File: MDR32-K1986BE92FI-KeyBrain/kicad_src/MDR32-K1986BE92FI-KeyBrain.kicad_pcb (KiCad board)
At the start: 2 copper layers, 18.1 x 33.3 mm, 34 parts, among them J1 USB-C USB 2.0 MC-372, J2 SWD, U1 AP2112K-3.3, U2 USBLC6-2SC6, U3 K1986BE92FI, U4 ProMicro, Y1 8MHz

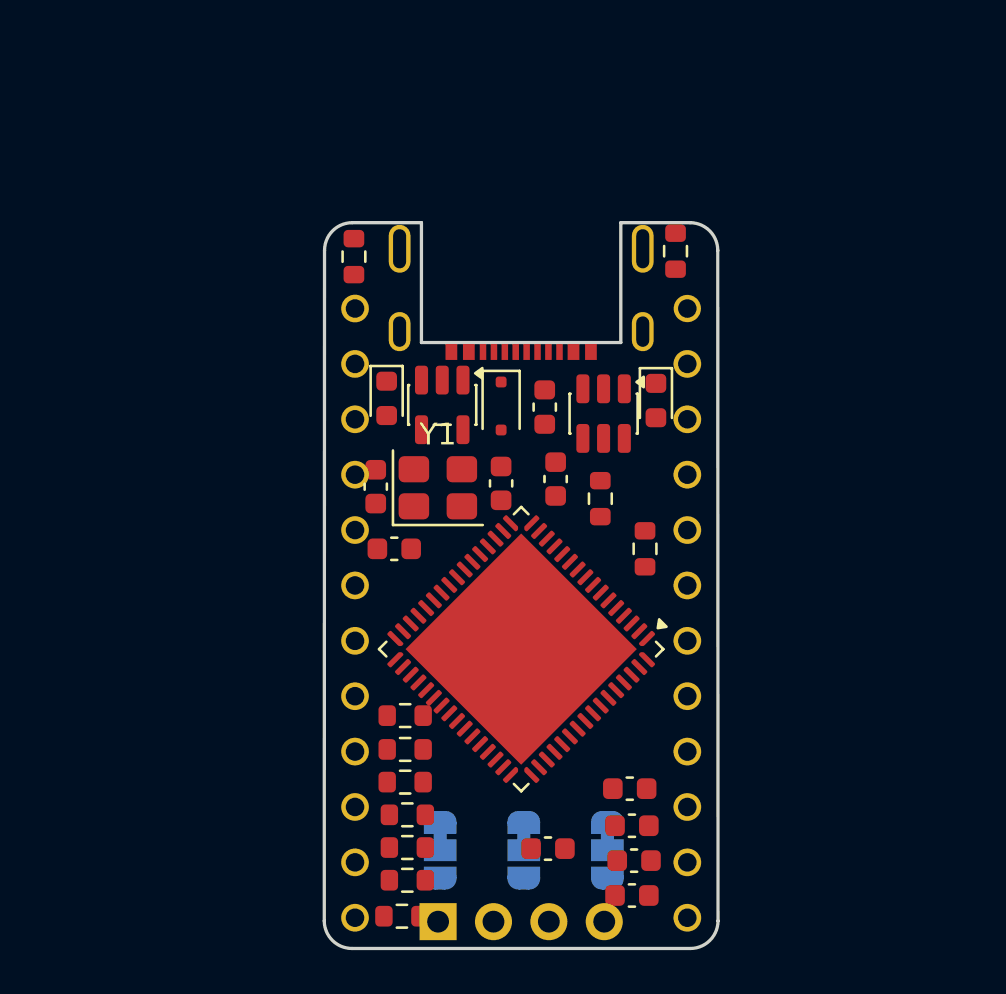
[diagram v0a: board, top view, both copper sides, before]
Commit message: MDR32-K1986BE92FI-KeyBrain: группируем и перепозиционируем
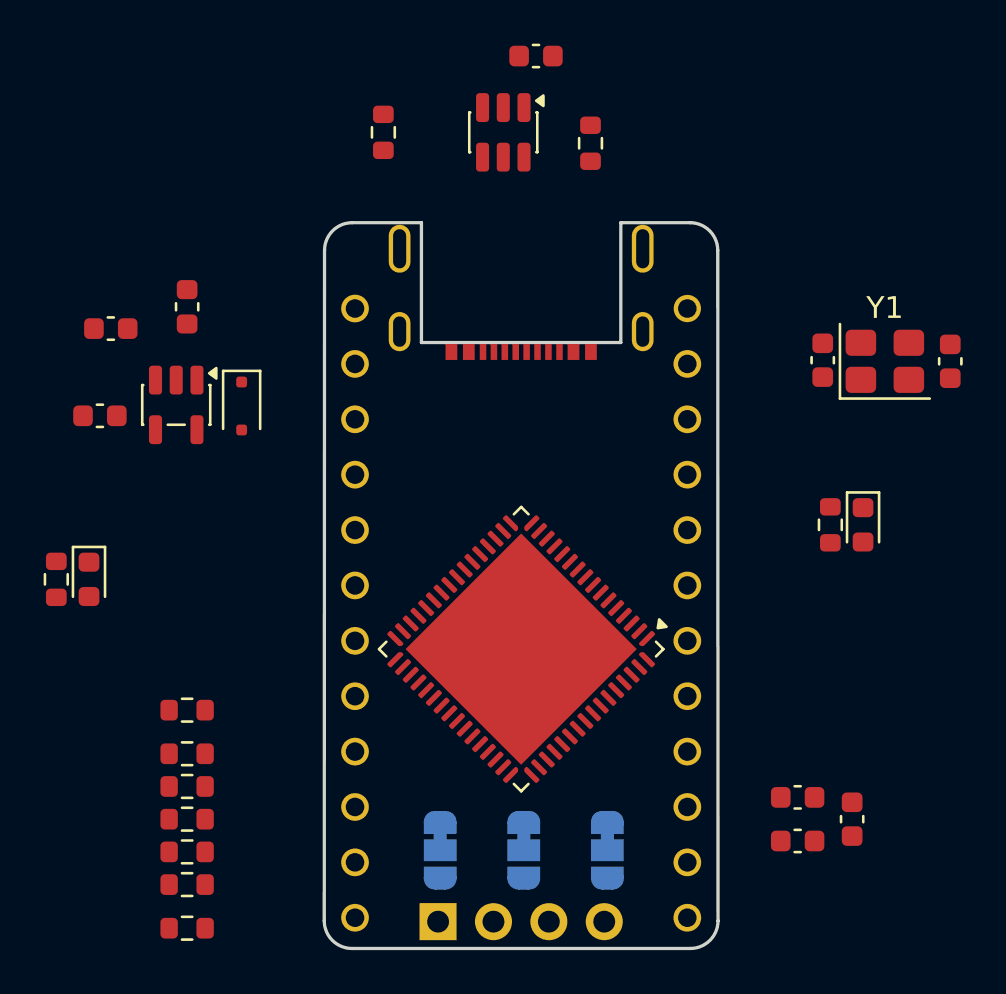
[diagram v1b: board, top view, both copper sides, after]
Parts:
- removed C12: 10pF, Capacitor_SMD:C_0603_1608Metric
- moved C4 38.8 mm to (81.5, 53.0)
- moved C1 33.0 mm to (62.0, 65.5)
- moved R10 25.2 mm to (59.5, 77.0)
- moved C5 24.5 mm to (100.5, 67.0), turned to -90 degrees
- moved C2 21.3 mm to (94.7, 67.0)
- moved Y1 21.3 mm to (97.5, 67.0)
- moved C7 20.7 mm to (96.0, 88.0)
- moved F1 17.0 mm to (65.5, 64.5)
- moved D2 16.0 mm to (61.0, 77.0)
- moved C3 14.8 mm to (61.5, 69.5)
- moved U2 13.7 mm to (80.0, 56.5)
- moved R2 12.4 mm to (65.5, 85.0)
- moved U1 12.2 mm to (65.0, 69.0)
- moved D1 11.9 mm to (68.0, 69.0)
- moved C8 11.7 mm to (93.5, 87.0)
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
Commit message: MDR32-K1986BE92FI-KeyBrain: частичное позиционирование
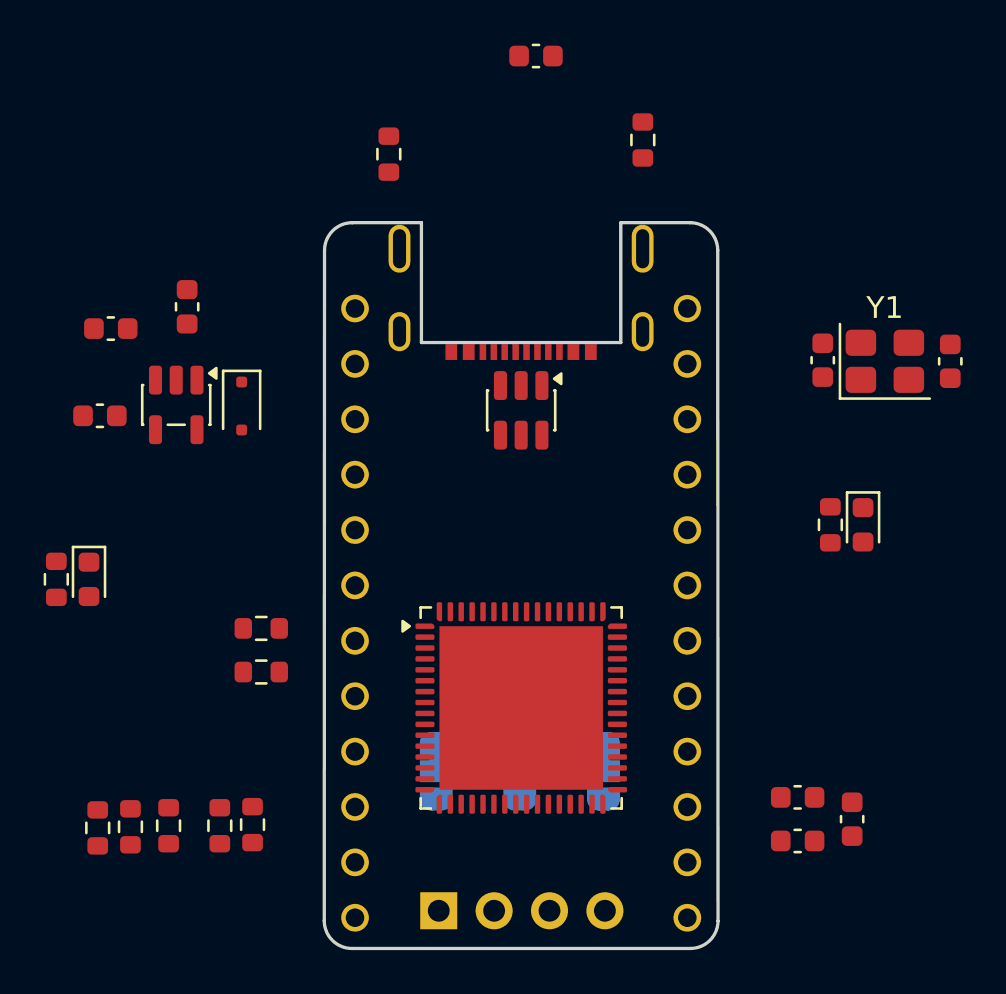
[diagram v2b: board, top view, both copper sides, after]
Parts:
- moved U2 12.8 mm to (80.8, 69.2)
- moved R6 12.2 mm to (68.9, 79.2)
- moved R7 12.2 mm to (68.9, 81.2)
- moved R9 11.9 mm to (86.4, 56.9)
- moved R8 9.26 mm to (74.8, 57.5)
- moved R1 5.51 mm to (67.0, 88.3), turned to 90 degrees
- moved R2 4.42 mm to (68.5, 88.2), turned to 90 degrees
- moved R5 4.24 mm to (61.4, 88.4), turned to 90 degrees
- moved JP1 3.63 mm to (76.9, 85.8)
- moved JP2 3.63 mm to (80.8, 85.8)
- moved JP3 3.63 mm to (84.6, 85.8)
- moved U3 2.70 mm to (80.8, 82.9), turned to 0 degrees
- moved R4 2.62 mm to (62.9, 88.3), turned to 90 degrees
- moved R3 1.99 mm to (64.7, 88.3), turned to 90 degrees
- moved J2 0.50 mm to (77.0, 92.2)
